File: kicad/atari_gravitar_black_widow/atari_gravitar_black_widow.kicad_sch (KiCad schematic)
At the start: 0 parts

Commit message: 4A DONE
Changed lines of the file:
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@@
     (effects (font (size 10.16 10.16) (thickness 2.032) bold) (justify left bottom))
+  )
+  (text "DONE" (at 246.38 227.838 0)
+    (effects (font (size 5.08 5.08) (thickness 1.016) bold) (justify left bottom))
+  )
+  (text "JBB\nDONE\nNeeds Review" (at 93.218 63.246 0)
+    (effects (font (size 5.08 5.08) (thickness 1.016) bold) (justify left bottom))
   )
   (text "DONE" (at 177.8 148.59 0)
@@
       (reference "#PWR?") (unit 1) (value "GND") (footprint "")
     )
+    (path "/00000000-0000-0000-0000-00006b1d2f90/20065448-9e3c-44d4-b86a-2c39f5a599db"
+      (reference "#PWR?") (unit 1) (value "GND") (footprint "")
+    )
     (path "/00000000-0000-0000-0000-00006b38237a/20848e94-15aa-4d25-a263-7ee5ee5fc2b0"
       (reference "#PWR?") (unit 1) (value "-15V") (footprint "")
@@
       (reference "#PWR?") (unit 1) (value "GND") (footprint "")
     )
+    (path "/00000000-0000-0000-0000-00006b1d2f90/238917f8-927e-47be-8566-55bd0b484043"
+      (reference "#PWR?") (unit 1) (value "GND") (footprint "")
+    )
     (path "/00000000-0000-0000-0000-00006b38237a/264061c8-c6f5-49cc-aff0-85da391a2951"
       (reference "#PWR?") (unit 1) (value "+6V") (footprint "")
@@
       (reference "#PWR?") (unit 1) (value "GND") (footprint "")
     )
+    (path "/00000000-0000-0000-0000-00006b1d2f90/3f5740c6-1ba7-4f13-87a4-8fb5519fc2c0"
+      (reference "#PWR?") (unit 1) (value "+5V") (footprint "")
+    )
     (path "/00000000-0000-0000-0000-00006b38237a/41c77165-c1d9-48c7-8d62-a625960a76fb"
+      (reference "#PWR?") (unit 1) (value "GND") (footprint "")
+    )
+    (path "/00000000-0000-0000-0000-00006b1d2f90/426122d9-db42-4f9d-8bda-a7361e5c7f0e"
       (reference "#PWR?") (unit 1) (value "GND") (footprint "")
     )
@@
       (reference "#PWR?") (unit 1) (value "-15V") (footprint "")
     )
+    (path "/00000000-0000-0000-0000-00006b1d2f90/4aca24e4-5550-4120-a940-73eef0229359"
+      (reference "#PWR?") (unit 1) (value "GND") (footprint "")
+    )
     (path "/00000000-0000-0000-0000-00006b38237a/4ce8f592-dd45-49f1-942a-f4c2c8b586ab"
       (reference "#PWR?") (unit 1) (value "GND") (footprint "")
@@
       (reference "#PWR?") (unit 1) (value "GND") (footprint "")
     )
+    (path "/00000000-0000-0000-0000-00006b1d2f90/60efd778-3860-4a32-bf01-a40a2e142227"
+      (reference "#PWR?") (unit 1) (value "+5V") (footprint "")
+    )
     (path "/00000000-0000-0000-0000-00006b38237a/648fff5d-0ca5-416c-b721-5f1de9429ea3"
       (reference "#PWR?") (unit 1) (value "GND") (footprint "")
@@
       (reference "#PWR?") (unit 1) (value "GND") (footprint "")
     )
+    (path "/00000000-0000-0000-0000-00006b1d2f90/b23ce53a-6fa3-4d27-b680-68122baf01c1"
+      (reference "#PWR?") (unit 1) (value "+5V") (footprint "")
+    )
     (path "/00000000-0000-0000-0000-00006b383070/b3b74159-32cf-457a-be4f-ee03f2c650b2"
       (reference "#PWR?") (unit 1) (value "+6V") (footprint "")
@@
       (reference "#PWR?") (unit 1) (value "-15V") (footprint "")
     )
+    (path "/00000000-0000-0000-0000-00006b1d2f90/c0d14d3f-e9f3-4573-98ea-8ab3e39434de"
+      (reference "#PWR?") (unit 1) (value "GND") (footprint "")
+    )
     (path "/00000000-0000-0000-0000-00006b383070/c2fd8df6-4d3c-4465-b1d8-7d79f259633e"
       (reference "#PWR?") (unit 1) (value "GND") (footprint "")
@@
       (reference "#PWR?") (unit 1) (value "-15V") (footprint "")
     )
+    (path "/00000000-0000-0000-0000-00006b1d2f90/ccd1a16b-2a46-490d-a077-4d19fa58cd15"
+      (reference "#PWR?") (unit 1) (value "GND") (footprint "")
+    )
     (path "/00000000-0000-0000-0000-00006b383070/d412d5a4-fc6f-47fe-8175-10d87422de2c"
       (reference "#PWR?") (unit 1) (value "+15V") (footprint "")
@@
       (reference "#PWR?") (unit 1) (value "GND") (footprint "")
     )
+    (path "/00000000-0000-0000-0000-00006b1d2f90/d7adfbb6-0c12-4e72-8dde-ffe92ef11c20"
+      (reference "#PWR?") (unit 1) (value "GND") (footprint "")
+    )
     (path "/00000000-0000-0000-0000-00006b383070/d89c71a7-2bfc-491c-bbe1-aa4a15a93355"
       (reference "#PWR?") (unit 1) (value "GND") (footprint "")
@@
     (path "/00000000-0000-0000-0000-00006b38237a/da65579c-0464-425e-877a-1272fea6e7e8"
       (reference "#PWR?") (unit 1) (value "GND") (footprint "")
+    )
+    (path "/00000000-0000-0000-0000-00006b1d2f90/dcbbf006-68d4-442a-9c24-44024ec1aa64"
+      (reference "#PWR?") (unit 1) (value "+5V") (footprint "")
     )
     (path "/00000000-0000-0000-0000-00006b38237a/de10cce6-b380-4cd7-9da0-7950eab6ae79"
@@
       (reference "#PWR?") (unit 1) (value "+15V") (footprint "")
     )
+    (path "/00000000-0000-0000-0000-00006b1d2f90/ed41916b-61bd-40d0-a069-b01ee3e76896"
+      (reference "#PWR?") (unit 1) (value "GND") (footprint "")
+    )
     (path "/00000000-0000-0000-0000-00006b38237a/f12c7c34-fc5e-4377-aaac-f66e352aaffd"
       (reference "#PWR?") (unit 1) (value "GND") (footprint "")
@@
       (reference "Q?") (unit 1) (value "2N3906") (footprint "quantum_arcade_pcb:GenTrans")
     )
+    (path "/00000000-0000-0000-0000-00006b1d2f90/fd61940d-7458-40cd-a231-2fe9aeb1770e"
+      (reference "R19") (unit 1) (value "1k") (footprint "quantum_arcade_pcb:GenComp")
+    )
     (path "/00000000-0000-0000-0000-00006b32d4fa/00000000-0000-0000-0000-00006b3d19fc"
       (reference "R20") (unit 1) (value "10K") (footprint "")
@@
       (reference "TP~WDDIS1") (unit 1) (value "TP") (footprint "")
     )
+    (path "/00000000-0000-0000-0000-00006b1d2f90/03fdd47f-b02f-4f8e-81d7-e58d5e8f3f9b"
+      (reference "U?") (unit 1) (value "LS138") (footprint "")
+    )
+    (path "/00000000-0000-0000-0000-00006b1d2f90/37d0f501-088e-4ffb-8284-414b1096acbe"
+      (reference "U?") (unit 1) (value "LS04") (footprint "")
+    )
+    (path "/00000000-0000-0000-0000-00006b1d2f90/3c8e5dad-4ffe-4955-a0b9-69d5211d5cde"
+      (reference "U?") (unit 1) (value "LS245") (footprint "")
+    )
+    (path "/00000000-0000-0000-0000-00006b1d2f90/77a083d5-904b-4dec-a1ce-d19ca39dd387"
+      (reference "U?") (unit 1) (value "6502") (footprint "")
+    )
+    (path "/00000000-0000-0000-0000-00006b1d2f90/94116d6b-353b-4db9-b2ad-ab301c1f8356"
+      (reference "U?") (unit 1) (value "LS244C") (footprint "")
+    )
     (path "/00000000-0000-0000-0000-00006b38237a/9b725e6a-c546-4be9-b734-41eb07658f4a"
       (reference "U?") (unit 1) (value "082A") (footprint "")
     )
+    (path "/00000000-0000-0000-0000-00006b1d2f90/b3a5dea4-176f-494f-906c-1153c3581d7a"
+      (reference "U?") (unit 1) (value "LS161") (footprint "")
+    )
+    (path "/00000000-0000-0000-0000-00006b1d2f90/c07df7ed-b483-4a92-a42f-26bc2a7c9197"
+      (reference "U?") (unit 1) (value "136010-X") (footprint "")
+    )
     (path "/00000000-0000-0000-0000-00006b38237a/d6ec0cf0-127a-46af-a57e-ad3a439f1567"
       (reference "U?") (unit 1) (value "LS273B") (footprint "")
     )
+    (path "/00000000-0000-0000-0000-00006b1d2f90/e846bbdf-157a-4553-851b-9974b522fd01"
+      (reference "U?") (unit 1) (value "LS244A") (footprint "")
+    )
+    (path "/00000000-0000-0000-0000-00006b1d2f90/f61301ac-cec2-413f-9166-d5cb86b0236d"
+      (reference "U?") (unit 1) (value "LS00") (footprint "")
+    )
     (path "/00000000-0000-0000-0000-00006b383070/f6cf73b9-5d6b-4b6f-a023-4748356d9b49"
       (reference "U?") (unit 1) (value "082A") (footprint "")
     )
+    (path "/00000000-0000-0000-0000-00006b1d2f90/fb8fe19d-e582-4275-9f60-82dea4bdbed9"
+      (reference "U?") (unit 1) (value "136010-X") (footprint "")
+    )
     (path "/00000000-0000-0000-0000-00006b383070/324ab83f-5e44-4ed2-9b62-345b75796455"
       (reference "U?") (unit 2) (value "082A") (footprint "")
     )
+    (path "/00000000-0000-0000-0000-00006b1d2f90/5bb2f273-dcb1-4131-8d44-371f164ab49d"
+      (reference "U?") (unit 2) (value "LS10") (footprint "")
+    )
     (path "/00000000-0000-0000-0000-00006b38237a/a70a24d9-1109-49fd-b298-e3575bfc1f71"
       (reference "U?") (unit 2) (value "082A") (footprint "")
     )
+    (path "/00000000-0000-0000-0000-00006b1d2f90/87a8507d-9093-412c-90b2-f02943538ea3"
+      (reference "U?") (unit 4) (value "LS00") (footprint "")
+    )
+    (path "/00000000-0000-0000-0000-00006b1d2f90/b2797f65-4bf6-4a46-8fe0-26a10af32575"
+      (reference "U?") (unit 4) (value "LS04") (footprint "")
+    )
+    (path "/00000000-0000-0000-0000-00006b1d2f90/6ffc1f17-3618-4ee7-a20d-a1171a936717"
+      (reference "U?") (unit 6) (value "LS04") (footprint "")
+    )
     (path "/00000000-0000-0000-0000-00006b0e57bf/00000000-0000-0000-0000-00006b3df6b2"

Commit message: 7B
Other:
- note added: "JBB IN PROGRESS"
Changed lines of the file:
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@@
+    (effects (font (size 5.08 5.08) (thickness 1.016) bold) (justify left bottom))
+  )
+  (text "JBB\nIN PROGRESS" (at 25.527 226.949 0)
     (effects (font (size 5.08 5.08) (thickness 1.016) bold) (justify left bottom))
   )

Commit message: 7B COMPLETED
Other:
- note removed: "JBB IN PROGRESS"

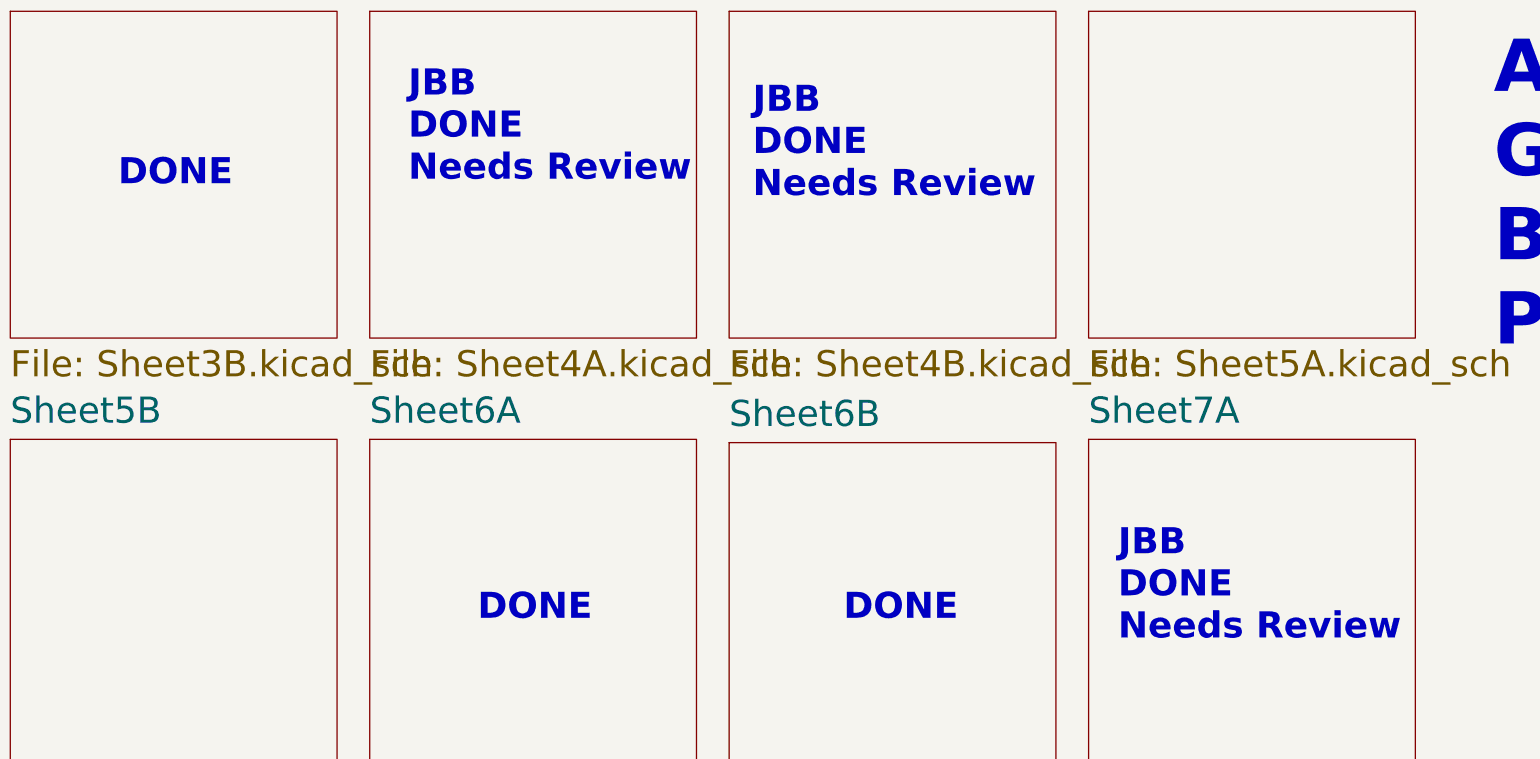
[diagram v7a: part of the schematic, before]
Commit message: Sheets 5A and 5B
Also subbed Φ for PHI in Φ2, BΦ2 and ~{BΦ2}
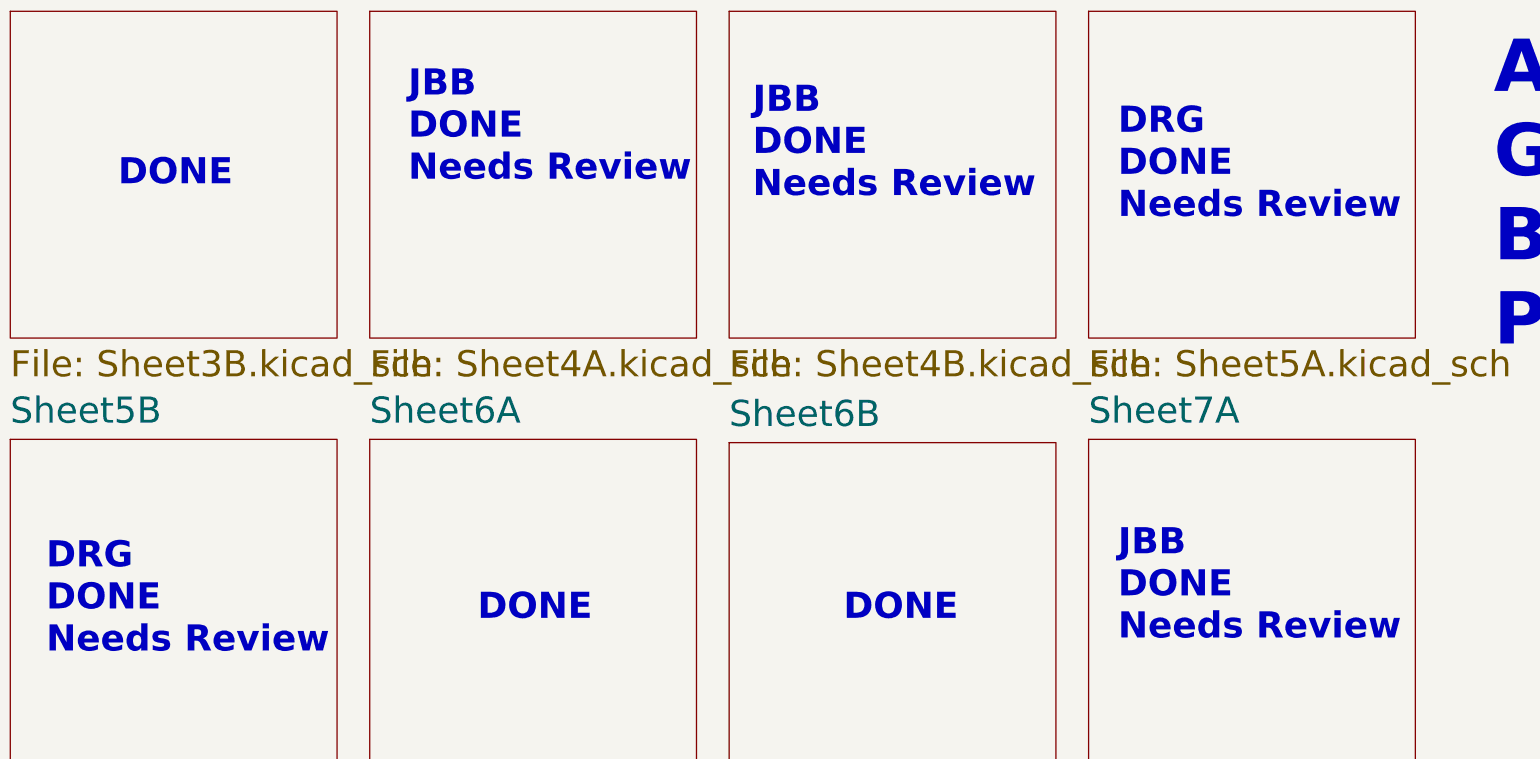
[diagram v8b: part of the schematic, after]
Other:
- note added: "DRG DONE Needs Review"
